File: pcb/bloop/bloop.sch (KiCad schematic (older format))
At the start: 0 parts

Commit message: Added schematic hierarchial sheets
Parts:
- added J?: TX, symbol Connector:Conn_Coaxial
- added J?: RX1, symbol Connector:Conn_Coaxial
- added J?: RX2, symbol Connector:Conn_Coaxial
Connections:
- new net GND: J?.2 (Ext), J?.2 (Ext), J?.2 (Ext)
- new net Radar MMIC and RF Front End/RX1: J?.1 (In)
- new net Radar MMIC and RF Front End/RX2: J?.1 (In)
- new net Radar MMIC and RF Front End/TX: J?.1 (In)
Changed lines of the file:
@@
 $Descr B 17000 11000
 encoding utf-8
-Sheet 1 1
+Sheet 1 5
 Title "Bloop Radar"
 Date ""
 Rev ""
 Comp ""
-Comment1 ""
-Comment2 ""
-Comment3 ""
-Comment4 ""
+Comment1 "Prabodh J."
+Comment2 "Leo L."
+Comment3 "Austin S."
+Comment4 "Design Engineers:"
 $EndDescr
+$Sheet
+S 10900 3400 2000 2000
+U 5D3D1319
+F0 "Interfaces" 50
+F1 "Interfaces.sch" 50
+$EndSheet
+$Sheet
+S 7400 6000 2000 1000
+U 5D3D147E
+F0 "Power" 50
+F1 "Power.sch" 50
+$EndSheet
+$Sheet
+S 3900 3400 2000 2000
+U 5D3D1628
+F0 "Radar MMIC and RF Front End" 50
+F1 "Radar_MMIC_RF_Front_End.sch" 50
+F2 "TX" O L 3900 3500 50
+F3 "RX1" I L 3900 4350 50
+F4 "RX2" I L 3900 5000 50
+$EndSheet
+$Sheet
+S 7400 3400 2000 2000
+U 5D3D17E1
+F0 "Baseband" 50
+F1 "Baseband.sch" 50
+$EndSheet
+$Comp
+L Connector:Conn_Coaxial J?
+U 1 1 5D3D972B
+P 2900 3500
+F 0 "J?" H 3100 3550 50  0000 C CNN
+F 1 "TX" H 3100 3450 50  0000 C CNN
+F 2 "" H 2900 3500 50  0001 C CNN
+F 3 " ~" H 2900 3500 50  0001 C CNN
+	1    2900 3500
+	-1   0    0    -1
+$EndComp
+$Comp
+L Connector:Conn_Coaxial J?
+U 1 1 5D3DB88B
+P 2900 4350
+F 0 "J?" H 3100 4400 50  0000 C CNN
+F 1 "RX1" H 3100 4300 50  0000 C CNN
+F 2 "" H 2900 4350 50  0001 C CNN
+F 3 " ~" H 2900 4350 50  0001 C CNN
+	1    2900 4350
+	-1   0    0    -1
+$EndComp
+Wire Wire Line
+	2900 3700 2900 3750
+$Comp
+L power:GND #PWR?
+U 1 1 5D3DC807
+P 2900 3750
+F 0 "#PWR?" H 2900 3500 50  0001 C CNN
+F 1 "GND" H 2905 3577 50  0000 C CNN
+F 2 "" H 2900 3750 50  0001 C CNN
+F 3 "" H 2900 3750 50  0001 C CNN
+	1    2900 3750
+	1    0    0    -1
+$EndComp
+$Comp
+L power:GND #PWR?
+U 1 1 5D3DC960
+P 2900 4600
+F 0 "#PWR?" H 2900 4350 50  0001 C CNN
+F 1 "GND" H 2905 4427 50  0000 C CNN
+F 2 "" H 2900 4600 50  0001 C CNN
+F 3 "" H 2900 4600 50  0001 C CNN
+	1    2900 4600
+	1    0    0    -1
+$EndComp
+Wire Wire Line
+	2900 4550 2900 4600
+$Comp
+L Connector:Conn_Coaxial J?
+U 1 1 5D3DE9B6
+P 2900 5000
+F 0 "J?" H 3100 5050 50  0000 C CNN
+F 1 "RX2" H 3100 4950 50  0000 C CNN
+F 2 "" H 2900 5000 50  0001 C CNN
+F 3 " ~" H 2900 5000 50  0001 C CNN
+	1    2900 5000
+	-1   0    0    -1
+$EndComp
+Wire Wire Line
+	2900 5200 2900 5250
+$Comp
+L power:GND #PWR?
+U 1 1 5D3DE9BD
+P 2900 5250
+F 0 "#PWR?" H 2900 5000 50  0001 C CNN
+F 1 "GND" H 2905 5077 50  0000 C CNN
+F 2 "" H 2900 5250 50  0001 C CNN
+F 3 "" H 2900 5250 50  0001 C CNN
+	1    2900 5250
+	1    0    0    -1
+$EndComp
+Wire Wire Line
+	3100 3500 3900 3500
+Wire Wire Line
+	3100 4350 3900 4350
+Wire Wire Line
+	3100 5000 3900 5000
 $EndSCHEMATC

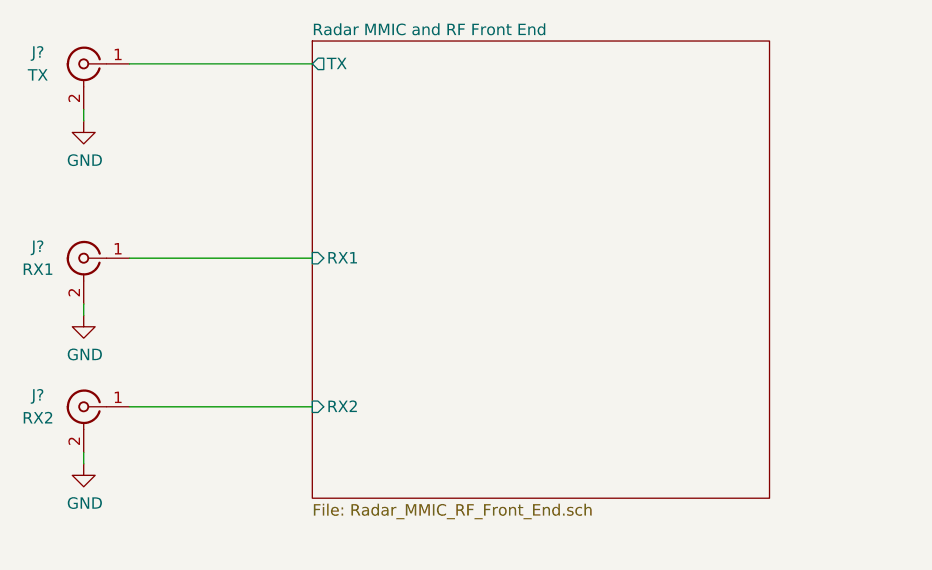
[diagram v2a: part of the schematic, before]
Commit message: Added BGT24MTR12 VQFN-32-9 footprint Updated gold material on 3d model 734153320
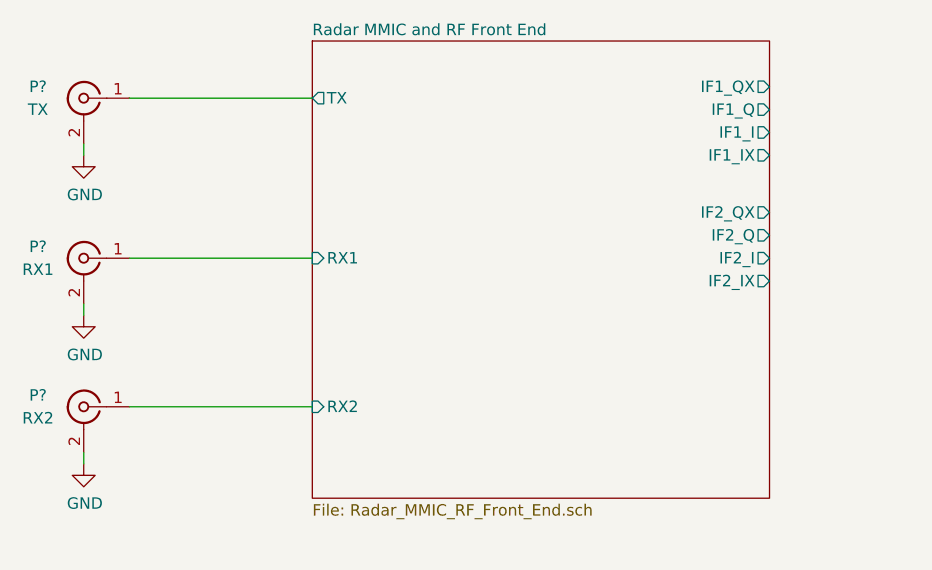
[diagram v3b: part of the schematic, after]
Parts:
- P? (x3): renamed from J?; footprint (none) -> bloop:0734153320; MPN (none) -> 0734153320
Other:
- moved on the sheet: P?
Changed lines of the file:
@@
 F0 "Radar MMIC and RF Front End" 50
 F1 "Radar_MMIC_RF_Front_End.sch" 50
-F2 "TX" O L 3900 3500 50
+F2 "TX" O L 3900 3650 50
 F3 "RX1" I L 3900 4350 50
 F4 "RX2" I L 3900 5000 50
+F5 "IF1_QX" O R 5900 3600 50
+F6 "IF1_Q" O R 5900 3700 50
+F7 "IF1_I" O R 5900 3800 50
+F8 "IF1_IX" O R 5900 3900 50
+F9 "IF2_QX" O R 5900 4150 50
+F10 "IF2_Q" O R 5900 4250 50
+F11 "IF2_I" O R 5900 4350 50
+F12 "IF2_IX" O R 5900 4450 50
 $EndSheet
 $Sheet
@@
 $EndSheet
 $Comp
-L Connector:Conn_Coaxial J?
+L Connector:Conn_Coaxial P?
 U 1 1 5D3D972B
-P 2900 3500
-F 0 "J?" H 3100 3550 50  0000 C CNN
-F 1 "TX" H 3100 3450 50  0000 C CNN
-F 2 "" H 2900 3500 50  0001 C CNN
-F 3 "https://www.molex.com/pdm_docs/sd/734153320_sd.pdf" H 2900 3500 50  0001 C CNN
-	1    2900 3500
+P 2900 3650
+F 0 "P?" H 3100 3700 50  0000 C CNN
+F 1 "TX" H 3100 3600 50  0000 C CNN
+F 2 "bloop:0734153320" H 2900 3650 50  0001 C CNN
+F 3 "https://www.molex.com/pdm_docs/sd/734153320_sd.pdf" H 2900 3650 50  0001 C CNN
+F 4 "0734153320" H 2900 3650 50  0001 C CNN "MPN"
+	1    2900 3650
 	-1   0    0    -1
 $EndComp
 $Comp
-L Connector:Conn_Coaxial J?
+L Connector:Conn_Coaxial P?
 U 1 1 5D3DB88B
 P 2900 4350
-F 0 "J?" H 3100 4400 50  0000 C CNN
+F 0 "P?" H 3100 4400 50  0000 C CNN
 F 1 "RX1" H 3100 4300 50  0000 C CNN
-F 2 "" H 2900 4350 50  0001 C CNN
+F 2 "bloop:0734153320" H 2900 4350 50  0001 C CNN
 F 3 "https://www.molex.com/pdm_docs/sd/734153320_sd.pdf" H 2900 4350 50  0001 C CNN
+F 4 "0734153320" H 2900 4350 50  0001 C CNN "MPN"
 	1    2900 4350
 	-1   0    0    -1
 $EndComp
 Wire Wire Line
-	2900 3700 2900 3750
+	2900 3850 2900 3900
 $Comp
 L power:GND #PWR?
 U 1 1 5D3DC807
-P 2900 3750
-F 0 "#PWR?" H 2900 3500 50  0001 C CNN
-F 1 "GND" H 2905 3577 50  0000 C CNN
-F 2 "" H 2900 3750 50  0001 C CNN
-F 3 "" H 2900 3750 50  0001 C CNN
-	1    2900 3750
+P 2900 3900
+F 0 "#PWR?" H 2900 3650 50  0001 C CNN
+F 1 "GND" H 2905 3727 50  0000 C CNN
+F 2 "" H 2900 3900 50  0001 C CNN
+F 3 "" H 2900 3900 50  0001 C CNN
+	1    2900 3900
 	1    0    0    -1
 $EndComp
@@
 	2900 4550 2900 4600
 $Comp
-L Connector:Conn_Coaxial J?
+L Connector:Conn_Coaxial P?
 U 1 1 5D3DE9B6
 P 2900 5000
-F 0 "J?" H 3100 5050 50  0000 C CNN
+F 0 "P?" H 3100 5050 50  0000 C CNN
 F 1 "RX2" H 3100 4950 50  0000 C CNN
-F 2 "" H 2900 5000 50  0001 C CNN
+F 2 "bloop:0734153320" H 2900 5000 50  0001 C CNN
 F 3 "https://www.molex.com/pdm_docs/sd/734153320_sd.pdf" H 2900 5000 50  0001 C CNN
+F 4 "0734153320" H 2900 5000 50  0001 C CNN "MPN"
 	1    2900 5000
 	-1   0    0    -1
@@
 $EndComp
 Wire Wire Line
-	3100 3500 3900 3500
+	3100 3650 3900 3650
 Wire Wire Line
 	3100 4350 3900 4350
